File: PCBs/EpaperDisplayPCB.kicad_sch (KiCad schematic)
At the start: 21 parts, among them J1 Conn_01x08, J2 Conn_01x12_FPC_0.5mm, Q1 AO3404A, U1 ePaper-2.1

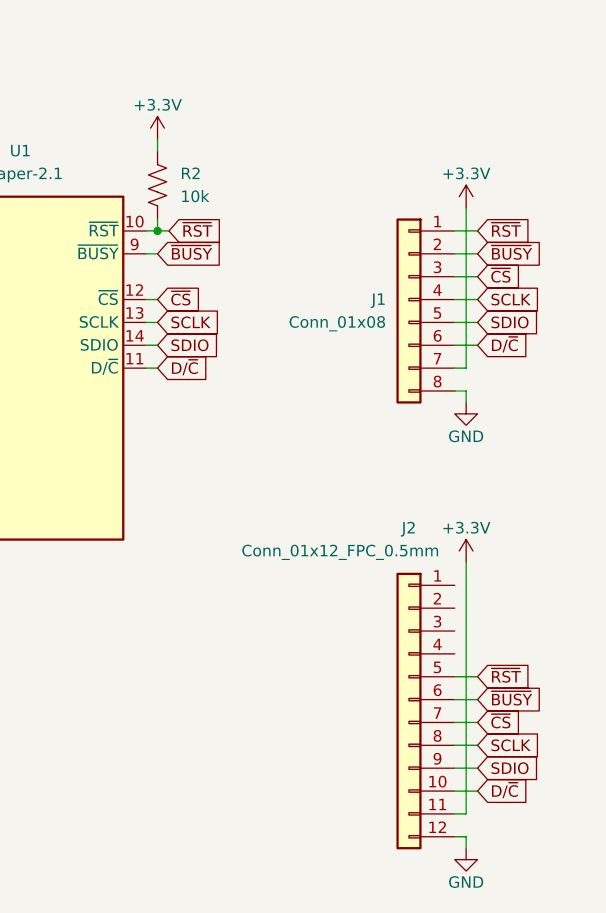
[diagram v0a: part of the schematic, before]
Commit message: Update Schematic
Epaper display schematic partial update
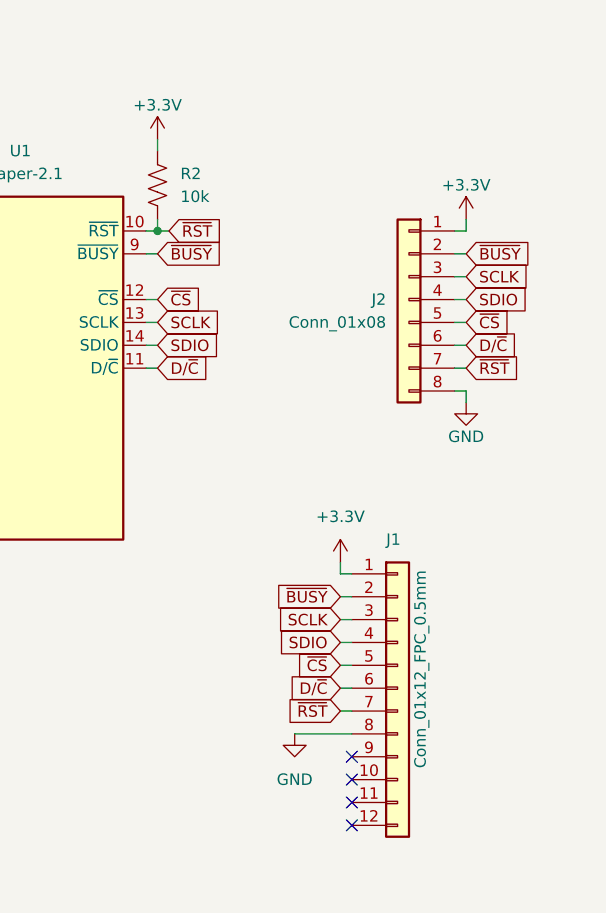
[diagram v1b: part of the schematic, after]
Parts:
- removed J2: Conn_01x12_FPC_0.5mm, SparkFun-Connector:FPC_12_0.5MM, symbol SparkFun-Connector:Conn_01x12_FPC_0.5mm
- added J1: Conn_01x12_FPC_0.5mm, SparkFun-Connector:FPC_12_0.5MM, symbol SparkFun-Connector:Conn_01x12_FPC_0.5mm
- renumbered J1 to J2
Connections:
- net +3.3V: now also J2.1 (Pin_1), J1.1 (Pin_1); no longer J2.7 (Pin_7)
- net D/~{C}: now also J1.6 (Pin_6)
- net GND: now also J1.8 (Pin_8)
- net SCLK: now also J2.3 (Pin_3), J1.3 (Pin_3); no longer J2.4 (Pin_4)
- net SDIO: now also J2.4 (Pin_4), J1.4 (Pin_4); no longer J2.5 (Pin_5)
- net ~{BUSY}: now also J1.2 (Pin_2)
- net ~{CS}: now also J2.5 (Pin_5), J1.5 (Pin_5); no longer J2.3 (Pin_3)
- net ~{RST}: now also J2.7 (Pin_7), J1.7 (Pin_7); no longer J2.1 (Pin_1)
- no-connect marks 0 -> 4

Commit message: Updates
Fixing connections between epaper display board and main board pcbs
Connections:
- net +3.3V: now also U1.7 (VDD); no longer U1.16 (VDD)
- net D/~{C}: now also J1.4 (Pin_4), J2.4 (Pin_4); no longer J1.6 (Pin_6), J2.6 (Pin_6)
- net SCLK: now also J1.6 (Pin_6), J2.6 (Pin_6); no longer J1.3 (Pin_3), J2.3 (Pin_3)
- net SDIO: now also J1.7 (Pin_7), J2.7 (Pin_7); no longer J1.4 (Pin_4), J2.4 (Pin_4)
- net ~{RST}: now also J1.3 (Pin_3), J2.3 (Pin_3); no longer J1.7 (Pin_7), J2.7 (Pin_7)
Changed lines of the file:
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@@
     (effects (font (size 2.54 2.54) (thickness 0.254) bold) (justify left bottom))
   )
-  (global_label "SDIO" (shape input) (at 215.9 115.57 180) (fields_autoplaced)
-    (effects (font (size 1.27 1.27)) (justify right))
-    (property "Intersheetrefs" "${INTERSHEET_REFS}" (at 208.5 115.57 0)
-      (effects (font (size 1.27 1.27)) (justify right) hide)
+  (global_label "SDIO" (shape input) (at 229.87 85.09 0) (fields_autoplaced)
+    (effects (font (size 1.27 1.27)) (justify left))
+    (property "Intersheetrefs" "${INTERSHEET_REFS}" (at 237.27 85.09 0)
+      (effects (font (size 1.27 1.27)) (justify left) hide)
+    )
+  )
+  (global_label "SCLK" (shape input) (at 229.87 82.55 0) (fields_autoplaced)
+    (effects (font (size 1.27 1.27)) (justify left))
+    (property "Intersheetrefs" "${INTERSHEET_REFS}" (at 237.6328 82.55 0)
+      (effects (font (size 1.27 1.27)) (justify left) hide)
+    )
+  )
+  (global_label "~{RST}" (shape input) (at 229.87 74.93 0) (fields_autoplaced)
+    (effects (font (size 1.27 1.27)) (justify left))
+    (property "Intersheetrefs" "${INTERSHEET_REFS}" (at 236.3023 74.93 0)
+      (effects (font (size 1.27 1.27)) (justify left) hide)
     )
   )
@@
     )
   )
-  (global_label "D{slash}~{C}" (shape input) (at 215.9 120.65 180) (fields_autoplaced)
-    (effects (font (size 1.27 1.27)) (justify right))
-    (property "Intersheetrefs" "${INTERSHEET_REFS}" (at 209.0443 120.65 0)
-      (effects (font (size 1.27 1.27)) (justify right) hide)
-    )
-  )
-  (global_label "~{RST}" (shape input) (at 229.87 85.09 0) (fields_autoplaced)
-    (effects (font (size 1.27 1.27)) (justify left))
-    (property "Intersheetrefs" "${INTERSHEET_REFS}" (at 236.3023 85.09 0)
-      (effects (font (size 1.27 1.27)) (justify left) hide)
-    )
-  )
-  (global_label "SDIO" (shape input) (at 229.87 77.47 0) (fields_autoplaced)
-    (effects (font (size 1.27 1.27)) (justify left))
-    (property "Intersheetrefs" "${INTERSHEET_REFS}" (at 237.27 77.47 0)
-      (effects (font (size 1.27 1.27)) (justify left) hide)
+  (global_label "D{slash}~{C}" (shape input) (at 215.9 115.57 180) (fields_autoplaced)
+    (effects (font (size 1.27 1.27)) (justify right))
+    (property "Intersheetrefs" "${INTERSHEET_REFS}" (at 209.0443 115.57 0)
+      (effects (font (size 1.27 1.27)) (justify right) hide)
     )
   )
@@
     )
   )
+  (global_label "SDIO" (shape input) (at 215.9 123.19 180) (fields_autoplaced)
+    (effects (font (size 1.27 1.27)) (justify right))
+    (property "Intersheetrefs" "${INTERSHEET_REFS}" (at 208.5 123.19 0)
+      (effects (font (size 1.27 1.27)) (justify right) hide)
+    )
+  )
   (global_label "~{BUSY}" (shape input) (at 215.9 110.49 180) (fields_autoplaced)
     (effects (font (size 1.27 1.27)) (justify right))
@@
     )
   )
-  (global_label "~{RST}" (shape input) (at 215.9 123.19 180) (fields_autoplaced)
-    (effects (font (size 1.27 1.27)) (justify right))
-    (property "Intersheetrefs" "${INTERSHEET_REFS}" (at 209.4677 123.19 0)
-      (effects (font (size 1.27 1.27)) (justify right) hide)
+  (global_label "D{slash}~{C}" (shape input) (at 229.87 77.47 0) (fields_autoplaced)
+    (effects (font (size 1.27 1.27)) (justify left))
+    (property "Intersheetrefs" "${INTERSHEET_REFS}" (at 236.7257 77.47 0)
+      (effects (font (size 1.27 1.27)) (justify left) hide)
     )
   )
@@
     )
   )
-  (global_label "SCLK" (shape input) (at 229.87 74.93 0) (fields_autoplaced)
-    (effects (font (size 1.27 1.27)) (justify left))
-    (property "Intersheetrefs" "${INTERSHEET_REFS}" (at 237.6328 74.93 0)
-      (effects (font (size 1.27 1.27)) (justify left) hide)
-    )
-  )
   (global_label "~{BUSY}" (shape input) (at 229.87 72.39 0) (fields_autoplaced)
     (effects (font (size 1.27 1.27)) (justify left))
@@
     )
   )
+  (global_label "SCLK" (shape input) (at 215.9 120.65 180) (fields_autoplaced)
+    (effects (font (size 1.27 1.27)) (justify right))
+    (property "Intersheetrefs" "${INTERSHEET_REFS}" (at 208.1372 120.65 0)
+      (effects (font (size 1.27 1.27)) (justify right) hide)
+    )
+  )
+  (global_label "~{RST}" (shape input) (at 215.9 113.03 180) (fields_autoplaced)
+    (effects (font (size 1.27 1.27)) (justify right))
+    (property "Intersheetrefs" "${INTERSHEET_REFS}" (at 209.4677 113.03 0)
+      (effects (font (size 1.27 1.27)) (justify right) hide)
+    )
+  )
   (global_label "~{BUSY}" (shape input) (at 195.58 72.39 0) (fields_autoplaced)
     (effects (font (size 1.27 1.27)) (justify left))
@@
     )
   )
-  (global_label "SCLK" (shape input) (at 215.9 113.03 180) (fields_autoplaced)
-    (effects (font (size 1.27 1.27)) (justify right))
-    (property "Intersheetrefs" "${INTERSHEET_REFS}" (at 208.1372 113.03 0)
-      (effects (font (size 1.27 1.27)) (justify right) hide)
-    )
-  )
   (global_label "~{RST}" (shape input) (at 196.85 69.85 0) (fields_autoplaced)
     (effects (font (size 1.27 1.27)) (justify left))
     (property "Intersheetrefs" "${INTERSHEET_REFS}" (at 203.2823 69.85 0)
-      (effects (font (size 1.27 1.27)) (justify left) hide)
-    )
-  )
-  (global_label "D{slash}~{C}" (shape input) (at 229.87 82.55 0) (fields_autoplaced)
-    (effects (font (size 1.27 1.27)) (justify left))
-    (property "Intersheetrefs" "${INTERSHEET_REFS}" (at 236.7257 82.55 0)
       (effects (font (size 1.27 1.27)) (justify left) hide)
     )
@@
     (pin "14")
     (pin "15")
-    (pin "16")
+    (pin "7")
     (pin "17")
     (pin "18")
@@
     (pin "5")
     (pin "6")
-    (pin "7")
+    (pin "16")
     (pin "8")
     (pin "9")

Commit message: Updates
Screen PCB updates
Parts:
- removed U1: ePaper-2.1, SparkFun-Display:ePaper-2.13, symbol SparkFun-Display:ePaper-2.1
- added FID1, FID2, FID3, FID4: Fiducial_0.5mm, SparkFun-Aesthetic:Fiducial_0.5mm_Mask1mm, symbol SparkFun-Aesthetic:Fiducial_0.5mm
- added U1: ePaper-2.13, SparkFun-Display:ePaper-2.13, symbol SparkFun-Display:ePaper-2.13
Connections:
- net +3.3V: now also U1.15 (VDDIO), U1.7 (VDD)
- net D/~{C}: now also U1.11 (D/~{C})
- net GND: now also U1.17 (GND), U1.8 (BS)
- net SCLK: now also U1.13 (SCLK)
- net SDIO: now also U1.14 (SDIO)
- net ~{BUSY}: now also U1.9 (~{BUSY})
- net ~{CS}: now also U1.12 (~{CS})
- net ~{RST}: now also U1.10 (~{RST})
- net at C5.1, D2.A: now also U1.23 (VGL)
- net at C4.1, D3.C: now also U1.21 (VGH)
- net at C8.1: now also U1.20 (VDH)
- net at C7.1: now also U1.18 (VDDD)
- net at Q1.1 (G): now also U1.2 (GDR)
- net at C9.1: now also U1.22 (VDL)
- net at C10.1: now also U1.24 (VCOM)
- net at Q1.2 (S), R1.2: now also U1.3 (RESE)
- net at C6.1: now also U1.5 (VDHR)
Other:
- note added: "Connectors"
- note added: "Fiducials"
- moved on the sheet: J1, J2

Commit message: Updated Epaper Display
Updated Epaper Display with new schematic symbol and placed the correct footprint onto the PCB
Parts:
- removed U1: ePaper-2.13, SparkFun-Display:ePaper-2.13, symbol SparkFun-Display:ePaper-2.13
- added U1: ePaper-2.66, SparkFun-Display:ePaper-2.66, symbol SparkFun-Display:ePaper-2.66
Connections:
- net +3.3V: now also U1.15 (VDDIO), U1.7 (VDD)
- net D/~{C}: now also U1.11 (D/~{C})
- net GND: now also U1.17 (GND), U1.8 (BS)
- net SCLK: now also U1.13 (SCLK)
- net SDIO: now also U1.14 (SDIO)
- net ~{BUSY}: now also U1.9 (~{BUSY})
- net ~{CS}: now also U1.12 (~{CS})
- net ~{RST}: now also U1.10 (~{RST})
- net at C5.1, D2.A: now also U1.23 (VGL)
- net at C4.1, D3.C: now also U1.21 (VGH)
- net at C8.1: now also U1.20 (VDH)
- net at C10.1: now also U1.24 (VCOM)
- net at C7.1: now also U1.18 (VDDD)
- net at Q1.1 (G): now also U1.2 (GDR)
- net at C9.1: now also U1.22 (VDL)
- net at Q1.2 (S), R1.2: now also U1.3 (RESE)
- net at C6.1: now also U1.5 (VDHR)

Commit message: epaper update
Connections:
- net +3.3V: now also U1.16 (VDD); no longer U1.7 (VDD)

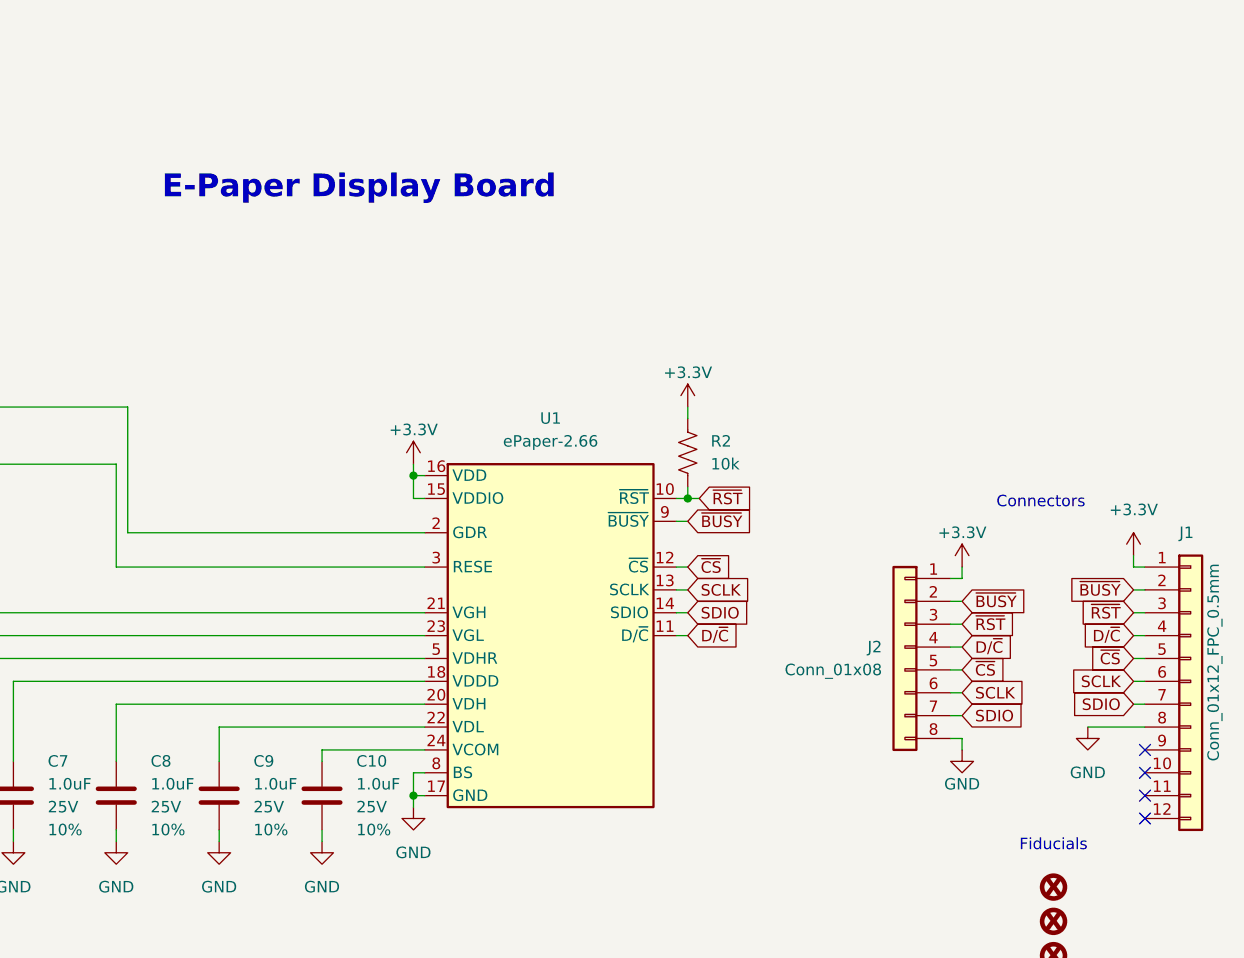
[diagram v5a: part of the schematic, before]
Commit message: Current PCB updates
Updated Main Board MQ sensors and external reset button position as well as SEN 55 connector pinout.
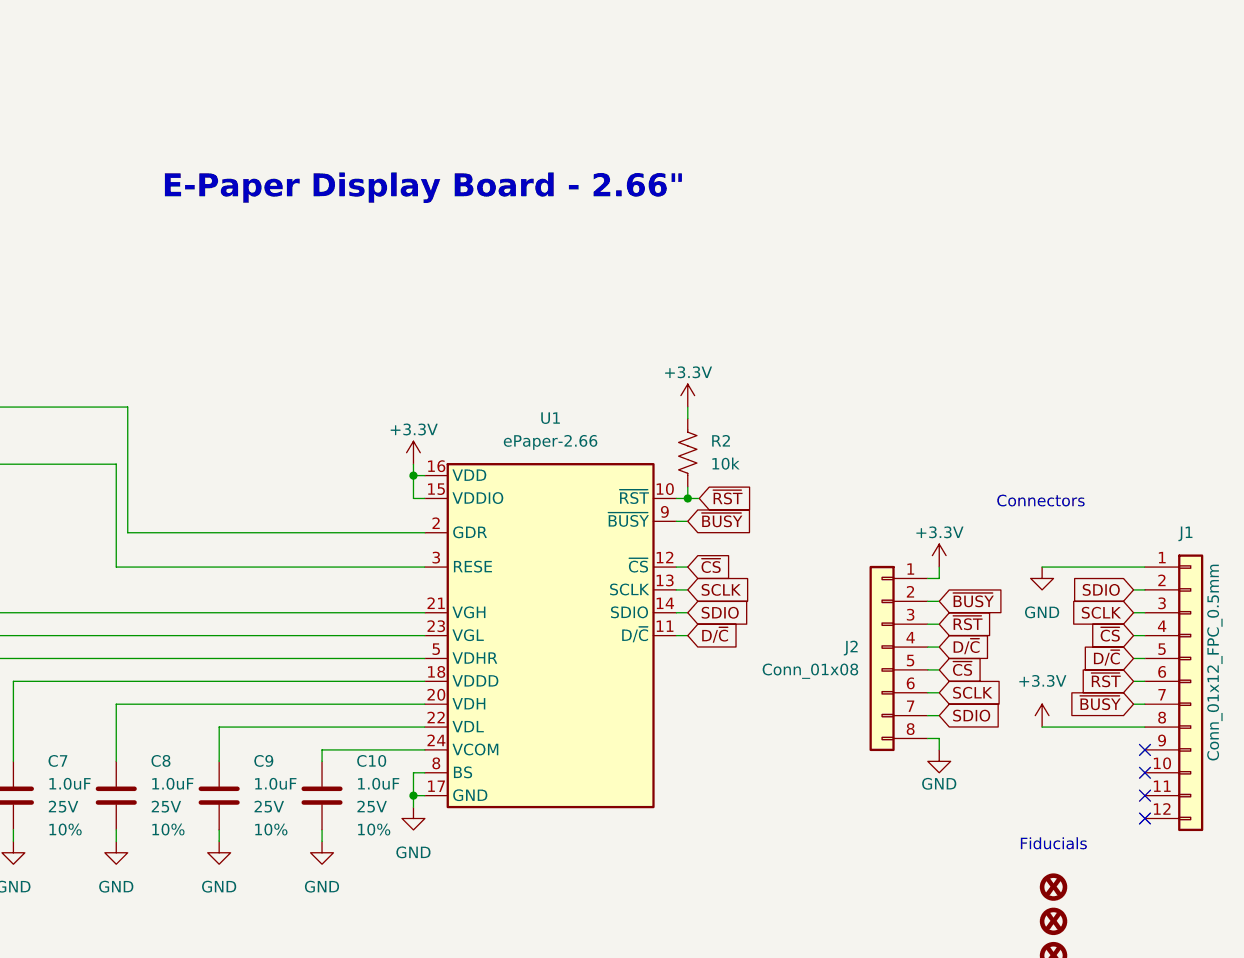
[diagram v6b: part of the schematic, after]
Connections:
- net +3.3V: now also J1.8 (Pin_8); no longer J1.1 (Pin_1)
- net D/~{C}: now also J1.5 (Pin_5); no longer J1.4 (Pin_4)
- net GND: now also J1.1 (Pin_1); no longer J1.8 (Pin_8)
- net SCLK: now also J1.3 (Pin_3); no longer J1.6 (Pin_6)
- net SDIO: now also J1.2 (Pin_2); no longer J1.7 (Pin_7)
- net ~{BUSY}: now also J1.7 (Pin_7); no longer J1.2 (Pin_2)
- net ~{CS}: now also J1.4 (Pin_4); no longer J1.5 (Pin_5)
- net ~{RST}: now also J1.6 (Pin_6); no longer J1.3 (Pin_3)
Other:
- note added: "E-Paper Display Board - 2.66""
- note removed: "E-Paper Display Board"
- moved on the sheet: J2
